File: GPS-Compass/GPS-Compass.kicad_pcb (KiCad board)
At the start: 2 copper layers, 100 x 78.5 mm, 70 parts, among them IC1 TPS565242DRLR, J2 USB_TypeC, Q3 Q_NMOS_GSD, U1 ESP32-S3-WROOM-1, U2 AP62300Z6, U3 BQ25887, U4 DRV8834RGER, U9 USBLC6-2SC6

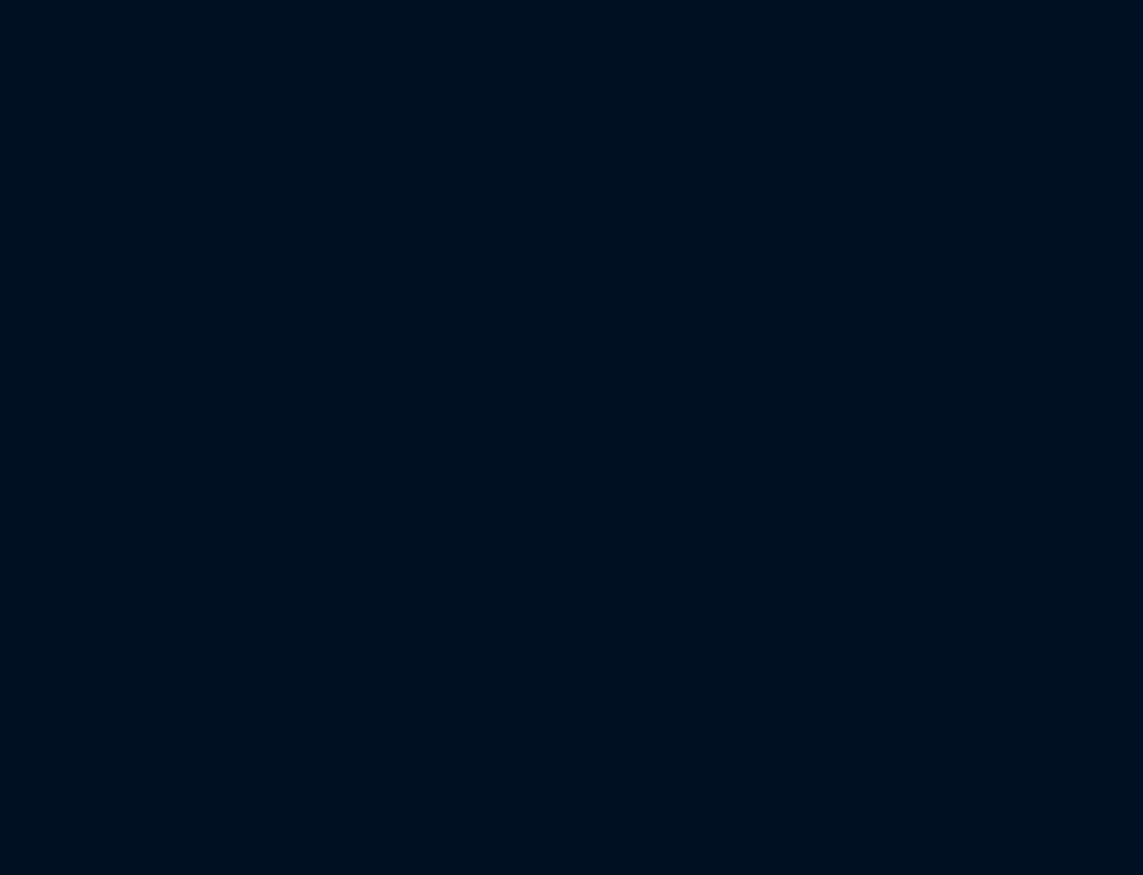
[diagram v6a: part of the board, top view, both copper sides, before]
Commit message: schematic remake
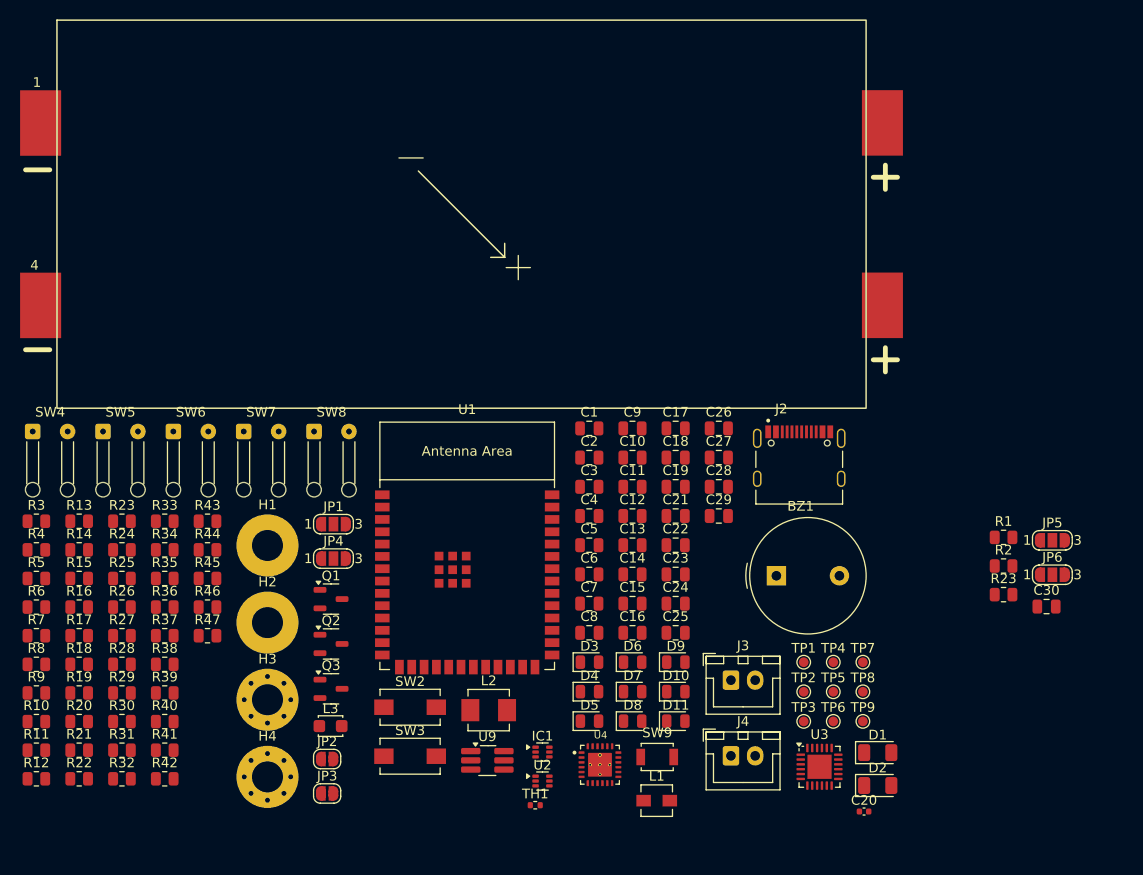
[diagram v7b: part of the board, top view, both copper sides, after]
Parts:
- added BT1: 2xLi-Ion_cells, gps-compass_brd:18650_2S_Holder, F.Cu at (-61.4, 34.9)
- added BZ1: Buzzer, gps-compass_brd:CEM-1203_Buzzer, F.Cu at (-25.6, 72.1)
- added C1: 100n, Capacitor_SMD:C_0805_2012Metric, F.Cu at (-48.2, 56.9)
- added C10: 10u, Capacitor_SMD:C_0805_2012Metric, F.Cu at (-43.7, 59.9)
- added C11: 22u, Capacitor_SMD:C_0805_2012Metric, F.Cu at (-43.7, 63.0)
- added C12: 22u, Capacitor_SMD:C_0805_2012Metric, F.Cu at (-43.7, 66.0)
- added C13: 1u, Capacitor_SMD:C_0805_2012Metric, F.Cu at (-43.7, 69.0)
- added C14: 47n, Capacitor_SMD:C_0805_2012Metric, F.Cu at (-43.7, 72.0)
- added C15: 4.7u, Capacitor_SMD:C_0805_2012Metric, F.Cu at (-43.7, 75.0)
- added C16: 10u, Capacitor_SMD:C_0805_2012Metric, F.Cu at (-43.7, 78.0)
- added C17: 10u, Capacitor_SMD:C_0805_2012Metric, F.Cu at (-39.3, 56.9)
- added C18: 22u, Capacitor_SMD:C_0805_2012Metric, F.Cu at (-39.3, 59.9)
- added C19: 10u, Capacitor_SMD:C_0805_2012Metric, F.Cu at (-39.3, 63.0)
- added C2: 100n, Capacitor_SMD:C_0805_2012Metric, F.Cu at (-48.2, 59.9)
- added C20: 10n, Capacitor_SMD:C_0402_1005Metric, F.Cu at (-19.9, 96.4)
- added C21: 100n, Capacitor_SMD:C_0805_2012Metric, F.Cu at (-39.3, 66.0)
- added C22: 100n, Capacitor_SMD:C_0805_2012Metric, F.Cu at (-39.3, 69.0)
- added C23: 44u, Capacitor_SMD:C_0805_2012Metric, F.Cu at (-39.3, 72.0)
- added C24: 100n, Capacitor_SMD:C_0805_2012Metric, F.Cu at (-39.3, 75.0)
- added C25: 100n, Capacitor_SMD:C_0805_2012Metric, F.Cu at (-39.3, 78.0)
- added C26: 100n, Capacitor_SMD:C_0805_2012Metric, F.Cu at (-34.8, 56.9)
- added C27: 100n, Capacitor_SMD:C_0805_2012Metric, F.Cu at (-34.8, 59.9)
- added C28: 100n, Capacitor_SMD:C_0805_2012Metric, F.Cu at (-34.8, 63.0)
- added C29: 100nF, Capacitor_SMD:C_0805_2012Metric, F.Cu at (-34.8, 66.0)
- added C3: 10u, Capacitor_SMD:C_0805_2012Metric, F.Cu at (-48.2, 63.0)
- added C30: 100n, Capacitor_SMD:C_0805_2012Metric, F.Cu at (-1.05, 75.3)
- added C4: 22u, Capacitor_SMD:C_0805_2012Metric, F.Cu at (-48.2, 66.0)
- added C5: 100n, Capacitor_SMD:C_0805_2012Metric, F.Cu at (-48.2, 69.0)
- added C6: 100n, Capacitor_SMD:C_0805_2012Metric, F.Cu at (-48.2, 72.0)
- added C7: 100n, Capacitor_SMD:C_0805_2012Metric, F.Cu at (-48.2, 75.0)
- added C8: 22u, Capacitor_SMD:C_0805_2012Metric, F.Cu at (-48.2, 78.0)
- added C9: 100n, Capacitor_SMD:C_0805_2012Metric, F.Cu at (-43.7, 56.9)
- added D1: D_Schottky, Diode_SMD:D_1206_3216Metric, F.Cu at (-18.4, 90.4)
- added D10: LED, LED_SMD:LED_0805_2012Metric, F.Cu at (-39.3, 84.1)
- added D11: LED, LED_SMD:LED_0805_2012Metric, F.Cu at (-39.3, 87.1)
- added D2: D_Schottky, Diode_SMD:D_1206_3216Metric, F.Cu at (-18.4, 93.7)
- added D3: LED, LED_SMD:LED_0805_2012Metric, F.Cu at (-48.2, 81.0)
- added D4: LED, LED_SMD:LED_0805_2012Metric, F.Cu at (-48.2, 84.1)
- added D5: LED, LED_SMD:LED_0805_2012Metric, F.Cu at (-48.2, 87.1)
- added D6: LED, LED_SMD:LED_0805_2012Metric, F.Cu at (-43.7, 81.0)
- added D7: LED, LED_SMD:LED_0805_2012Metric, F.Cu at (-43.7, 84.1)
- added D8: LED, LED_SMD:LED_0805_2012Metric, F.Cu at (-43.7, 87.1)
- added D9: LED, LED_SMD:LED_0805_2012Metric, F.Cu at (-39.3, 81.0)
- added H1: Mounting Hole M3, MountingHole:MountingHole_3.2mm_M3_Pad, F.Cu at (-81.3, 69.0)
- added H2: Mounting Hole M3, MountingHole:MountingHole_3.2mm_M3_Pad, F.Cu at (-81.3, 77.0)
- added H3: Mounting Hole M3, MountingHole:MountingHole_3.2mm_M3_Pad_Via, F.Cu at (-81.3, 84.9)
- added H4: Mounting Hole M3, MountingHole:MountingHole_3.2mm_M3_Pad_Via, F.Cu at (-81.3, 92.9)
- added IC1: TPS565242DRLR, Package_TO_SOT_SMD:SOT-563, F.Cu at (-53.0, 90.3)
- added J2: USB_TypeC, sumec_brd:HRO_TYPE-C-31-M-12, F.Cu at (-26.5, 62.1)
- added J3: Conn_01x02_Pin, Connector_JST:JST_XH_B2B-XH-A_1x02_P2.50mm_Vertical, F.Cu at (-33.6, 82.9)
- added J4: Conn_01x02_Pin, Connector_JST:JST_XH_B2B-XH-A_1x02_P2.50mm_Vertical, F.Cu at (-33.6, 90.7)
- added JP1: Jumper, Jumper:SolderJumper-3_P1.3mm_Open_RoundedPad1.0x1.5mm_NumberLabels, F.Cu at (-74.5, 66.8)
- added JP2: Jumper, Jumper:SolderJumper-2_P1.3mm_Open_RoundedPad1.0x1.5mm, F.Cu at (-75.2, 91.0)
- added JP3: Jumper, Jumper:SolderJumper-2_P1.3mm_Open_RoundedPad1.0x1.5mm, F.Cu at (-75.2, 94.6)
- added JP4: Jumper, Jumper:SolderJumper-3_P1.3mm_Open_RoundedPad1.0x1.5mm_NumberLabels, F.Cu at (-74.5, 70.4)
- added JP5: Jumper, Jumper:SolderJumper-3_P1.3mm_Open_RoundedPad1.0x1.5mm_NumberLabels, F.Cu at (-0.45, 68.5)
- added JP6: Jumper, Jumper:SolderJumper-3_P1.3mm_Open_RoundedPad1.0x1.5mm_NumberLabels, F.Cu at (-0.45, 72.0)
- added L1: 1.5u, Inductor_SMD:L_Vishay_IHLP-1212, F.Cu at (-41.2, 95.3)
- added L2: 3.3u, Inductor_SMD:L_Vishay_IHLP-1616, F.Cu at (-58.5, 86.0)
- added L3: 1u, Inductor_SMD:L_Walsin_WLFM201609x, F.Cu at (-74.8, 87.6)
- added Q1: Q_PMOS, Package_TO_SOT_SMD:SOT-23-3, F.Cu at (-74.8, 74.5)
- added Q2: Q_PMOS, Package_TO_SOT_SMD:SOT-23-3, F.Cu at (-74.8, 79.2)
- added Q3: NMOS, Package_TO_SOT_SMD:SOT-23-3, F.Cu at (-74.8, 83.8)
- added R1: 100k, Resistor_SMD:R_0805_2012Metric, F.Cu at (-5.48, 68.2)
- added R10: 10k, Resistor_SMD:R_0805_2012Metric, F.Cu at (-105.2, 87.2)
- added R11: 383R, Resistor_SMD:R_0805_2012Metric, F.Cu at (-105.2, 90.1)
- added R12: 300R, Resistor_SMD:R_0805_2012Metric, F.Cu at (-105.2, 93.1)
- added R13: 9.5R, Resistor_SMD:R_0805_2012Metric, F.Cu at (-100.8, 66.5)
- added R14: 10k, Resistor_SMD:R_0805_2012Metric, F.Cu at (-100.8, 69.5)
- added R15: 5.23k, Resistor_SMD:R_0805_2012Metric, F.Cu at (-100.8, 72.4)
- added R16: 30.1k, Resistor_SMD:R_0805_2012Metric, F.Cu at (-100.8, 75.4)
- added R17: R(SET), Resistor_SMD:R_0805_2012Metric, F.Cu at (-100.8, 78.3)
- added R18: R(SET), Resistor_SMD:R_0805_2012Metric, F.Cu at (-100.8, 81.3)
- added R19: 10k, Resistor_SMD:R_0805_2012Metric, F.Cu at (-100.8, 84.2)
- added R2: 10k, Resistor_SMD:R_0805_2012Metric, F.Cu at (-5.48, 71.1)
- added R20: 5.1k, Resistor_SMD:R_0805_2012Metric, F.Cu at (-100.8, 87.2)
- added R21: 10k, Resistor_SMD:R_0805_2012Metric, F.Cu at (-100.8, 90.1)
- added R22: 10k, Resistor_SMD:R_0805_2012Metric, F.Cu at (-100.8, 93.1)
- added R23: 45k, Resistor_SMD:R_0805_2012Metric, F.Cu at (-5.48, 74.1)
- added R23: 100k, Resistor_SMD:R_0805_2012Metric, F.Cu at (-96.3, 66.5)
- added R24: 10k, Resistor_SMD:R_0805_2012Metric, F.Cu at (-96.3, 69.5)
- added R25: 1k, Resistor_SMD:R_0805_2012Metric, F.Cu at (-96.3, 72.4)
- added R26: 1k, Resistor_SMD:R_0805_2012Metric, F.Cu at (-96.3, 75.4)
- added R27: 15R, Resistor_SMD:R_0805_2012Metric, F.Cu at (-96.3, 78.3)
- added R28: 15R, Resistor_SMD:R_0805_2012Metric, F.Cu at (-96.3, 81.3)
- added R29: 5.1k, Resistor_SMD:R_0805_2012Metric, F.Cu at (-96.3, 84.2)
- added R3: 45k, Resistor_SMD:R_0805_2012Metric, F.Cu at (-105.2, 66.5)
- added R30: 2.2k, Resistor_SMD:R_0805_2012Metric, F.Cu at (-96.3, 87.2)
- added R31: 2.2k, Resistor_SMD:R_0805_2012Metric, F.Cu at (-96.3, 90.1)
- added R32: 2.2k, Resistor_SMD:R_0805_2012Metric, F.Cu at (-96.3, 93.1)
- added R33: 10k, Resistor_SMD:R_0805_2012Metric, F.Cu at (-91.9, 66.5)
- added R34: 10k, Resistor_SMD:R_0805_2012Metric, F.Cu at (-91.9, 69.5)
- added R35: 10k, Resistor_SMD:R_0805_2012Metric, F.Cu at (-91.9, 72.4)
- added R36: 10k, Resistor_SMD:R_0805_2012Metric, F.Cu at (-91.9, 75.4)
- added R37: 220R, Resistor_SMD:R_0805_2012Metric, F.Cu at (-91.9, 78.3)
- added R38: 220R, Resistor_SMD:R_0805_2012Metric, F.Cu at (-91.9, 81.3)
- added R39: 220R, Resistor_SMD:R_0805_2012Metric, F.Cu at (-91.9, 84.2)
- added R4: 100k, Resistor_SMD:R_0805_2012Metric, F.Cu at (-105.2, 69.5)
- added R40: 0R, Resistor_SMD:R_0805_2012Metric, F.Cu at (-91.9, 87.2)
- added R41: 10k, Resistor_SMD:R_0805_2012Metric, F.Cu at (-91.9, 90.1)
- added R42: 10k, Resistor_SMD:R_0805_2012Metric, F.Cu at (-91.9, 93.1)
- added R43: 1k, Resistor_SMD:R_0805_2012Metric, F.Cu at (-87.5, 66.5)
- added R44: 10k, Resistor_SMD:R_0805_2012Metric, F.Cu at (-87.5, 69.5)
- added R45: 2.2k, Resistor_SMD:R_0805_2012Metric, F.Cu at (-87.5, 72.4)
- added R46: 2.2k, Resistor_SMD:R_0805_2012Metric, F.Cu at (-87.5, 75.4)
- added R47: 2.2k, Resistor_SMD:R_0805_2012Metric, F.Cu at (-87.5, 78.3)
- added R5: 52.3k, Resistor_SMD:R_0805_2012Metric, F.Cu at (-105.2, 72.4)
- added R6: 10k, Resistor_SMD:R_0805_2012Metric, F.Cu at (-105.2, 75.4)
- added R7: 10k, Resistor_SMD:R_0805_2012Metric, F.Cu at (-105.2, 78.3)
- added R8: 52.3k, Resistor_SMD:R_0805_2012Metric, F.Cu at (-105.2, 81.3)
- added R9: 10k, Resistor_SMD:R_0805_2012Metric, F.Cu at (-105.2, 84.2)
- added SW2: PROG, Button_Switch_SMD:SW_SPST_EVQPE1, F.Cu at (-66.7, 85.7)
- added SW3: PROG, Button_Switch_SMD:SW_SPST_EVQPE1, F.Cu at (-66.7, 90.7)
- added SW4: EXT, Connector_Wire:SolderWire-0.1sqmm_1x02_P3.6mm_D0.4mm_OD1mm_Relief, F.Cu at (-105.5, 57.3)
- added SW5: EXT, Connector_Wire:SolderWire-0.1sqmm_1x02_P3.6mm_D0.4mm_OD1mm_Relief, F.Cu at (-98.3, 57.3)
- added SW6: EXT, Connector_Wire:SolderWire-0.1sqmm_1x02_P3.6mm_D0.4mm_OD1mm_Relief, F.Cu at (-91.0, 57.3)
- added SW7: RESET, Connector_Wire:SolderWire-0.1sqmm_1x02_P3.6mm_D0.4mm_OD1mm_Relief, F.Cu at (-83.8, 57.3)
- added SW8: RESET, Connector_Wire:SolderWire-0.1sqmm_1x02_P3.6mm_D0.4mm_OD1mm_Relief, F.Cu at (-76.5, 57.3)
- added SW9: BOOT, Button_Switch_SMD:SW_SPST_B3U-1000P, F.Cu at (-41.2, 90.8)
- added TH1: 10k NTC, Resistor_SMD:R_0402_1005Metric, F.Cu at (-53.8, 95.8)
- added TP1: TestPoint, TestPoint:TestPoint_Pad_D1.0mm, F.Cu at (-26.1, 81.0)
- added TP2: TestPoint, TestPoint:TestPoint_Pad_D1.0mm, F.Cu at (-26.1, 84.1)
- added TP3: TestPoint, TestPoint:TestPoint_Pad_D1.0mm, F.Cu at (-26.1, 87.1)
- added TP4: TestPoint, TestPoint:TestPoint_Pad_D1.0mm, F.Cu at (-23.0, 81.0)
- added TP5: TestPoint, TestPoint:TestPoint_Pad_D1.0mm, F.Cu at (-23.0, 84.1)
- added TP6: TestPoint, TestPoint:TestPoint_Pad_D1.0mm, F.Cu at (-23.0, 87.1)
- added TP7: TestPoint, TestPoint:TestPoint_Pad_D1.0mm, F.Cu at (-20.0, 81.0)
- added TP8: TestPoint, TestPoint:TestPoint_Pad_D1.0mm, F.Cu at (-20.0, 84.1)
- added TP9: TestPoint, TestPoint:TestPoint_Pad_D1.0mm, F.Cu at (-20.0, 87.1)
- added U1: ESP32-S3-WROOM-1, PCM_Espressif:ESP32-S3-WROOM-1, F.Cu at (-60.8, 72.0)
- added U2: AP62300Z6, Package_TO_SOT_SMD:SOT-563, F.Cu at (-53.0, 93.3)
- added U3: BQ25887, Package_DFN_QFN:VQFN-24-1EP_4x4mm_P0.5mm_EP2.5x2.5mm, F.Cu at (-24.4, 91.8)
- added U4: DRV8834RGER, gps-compass_brd:DRIVER_DRV8834RGER, F.Cu at (-47.1, 91.6)
- added U9: USBLC6-2SC6, Package_TO_SOT_SMD:TSOT-23-6_HandSoldering, F.Cu at (-58.7, 91.2)
